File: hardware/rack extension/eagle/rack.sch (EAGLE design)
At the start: 48 parts, among them IC1 74ACT139N, IC2 74AC574N, IC3 74AC32N, IC4 74AC86N, IC5 74AC04N, IC6 74AC14N, IC7 74AC541N, K1 APF30212C, K2 APF30212C, Q1 BC547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

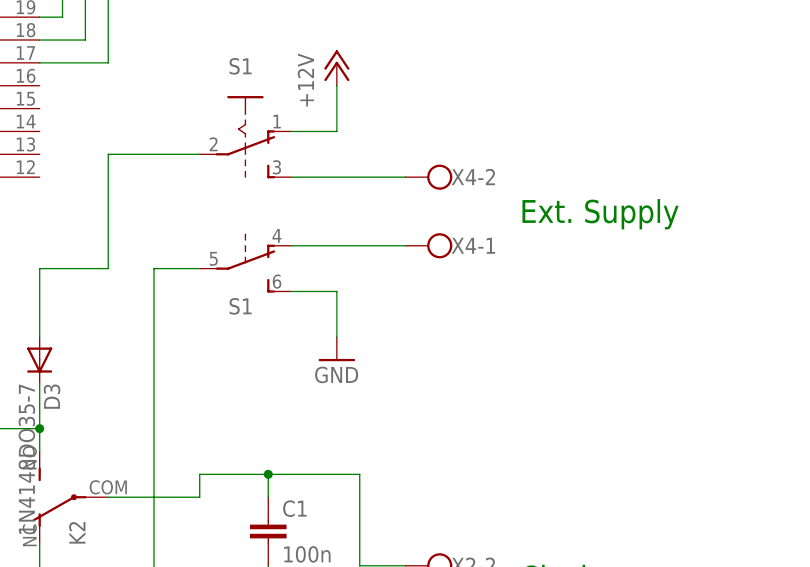
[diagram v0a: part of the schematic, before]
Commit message: Bad fail in rack hardware
The switch S1 was connected wrong so the change from internal to
external supply didnt work.
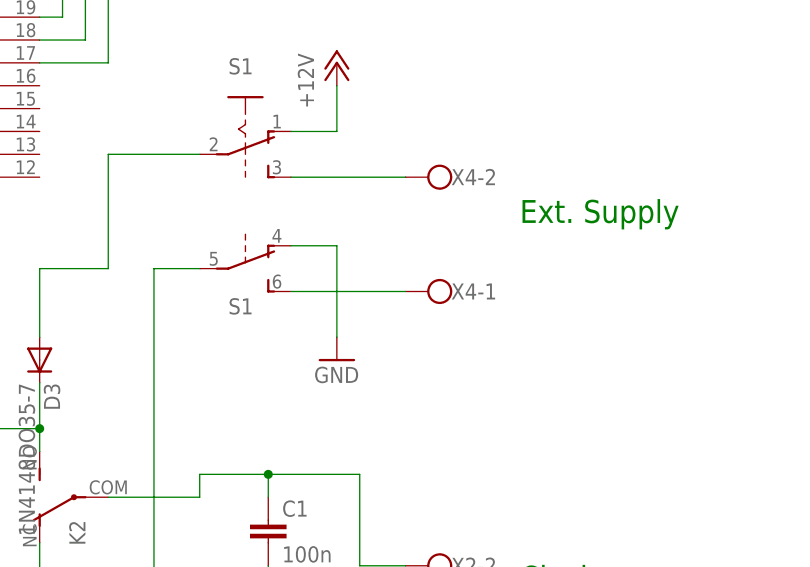
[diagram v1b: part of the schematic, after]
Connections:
- net GND: now also S1B.O; no longer S1B.S
- net N$33: now also S1B.S; no longer S1B.O
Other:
- moved on the sheet: X4-1
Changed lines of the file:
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@@
 <instance part="S1" gate="B" x="195.58" y="53.34" rot="R270"/>
 <instance part="S1" gate="A" x="195.58" y="68.58" rot="R270"/>
-<instance part="X4" gate="-1" x="218.44" y="55.88" rot="R180"/>
+<instance part="X4" gate="-1" x="218.44" y="50.8" rot="R180"/>
 <instance part="X4" gate="-2" x="218.44" y="63.5" rot="R180"/>
 <instance part="P+9" gate="1" x="152.4" y="27.94"/>
@@
 </segment>
 <segment>
-<pinref part="S1" gate="B" pin="S"/>
 <pinref part="GND9" gate="1" pin="GND"/>
-<wire x1="200.66" y1="50.8" x2="205.74" y2="50.8" width="0.1524" layer="91"/>
-<wire x1="205.74" y1="50.8" x2="205.74" y2="45.72" width="0.1524" layer="91"/>
+<wire x1="205.74" y1="45.72" x2="205.74" y2="55.88" width="0.1524" layer="91"/>
+<pinref part="S1" gate="B" pin="O"/>
+<wire x1="205.74" y1="55.88" x2="200.66" y2="55.88" width="0.1524" layer="91"/>
 </segment>
 <segment>
@@
 </segment>
 </net>
-<net name="N$33" class="0">
-<segment>
-<pinref part="S1" gate="B" pin="O"/>
-<pinref part="X4" gate="-1" pin="KL"/>
-<wire x1="200.66" y1="55.88" x2="213.36" y2="55.88" width="0.1524" layer="91"/>
-</segment>
-</net>
 <net name="N$34" class="0">
 <segment>
@@
 </segment>
 </net>
+<net name="N$33" class="0">
+<segment>
+<pinref part="S1" gate="B" pin="S"/>
+<pinref part="X4" gate="-1" pin="KL"/>
+<wire x1="200.66" y1="50.8" x2="213.36" y2="50.8" width="0.1524" layer="91"/>
+</segment>
+</net>

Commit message: Layout updated
Updated layout from rack extension
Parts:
- removed SV2: (no value), con-lstb:MA03-2
- added SV5: (no value), con-lstb:MA03-1
- C8: value (none) -> 2µ2
- IC1: value 74ACT139N -> 74HC139N; device 74xx-eu:74ACT139N -> 74xx-eu:74HC139N
- IC2: value 74AC574N -> 74HC574N; device 74xx-eu:74AC574N -> 74xx-eu:74HC574N
- IC3: value 74AC32N -> 74HC32N; device 74xx-eu:74AC32N -> 74xx-eu:74HC32N
- IC4: value 74AC86N -> 74HC86N; device 74xx-eu:74AC86N -> 74xx-eu:74HC86N
- IC5: value 74AC04N -> 74HC04N; device 74xx-eu:74AC04N -> 74xx-eu:74HC04N
- IC6: value 74AC14N -> 74HC14N; device 74xx-eu:74AC14N -> 74xx-eu:74HC14N
- IC7: value 74AC541N -> 74HC541N; device 74xx-eu:74AC541N -> 74xx-eu:74HC541N
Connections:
- net N$36: now also SV5.2; no longer SV2.3, SV2.5
- net N$6: now also SV5.3; no longer SV2.4
- net N$7: now also SV5.1; no longer SV2.6
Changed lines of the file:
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@@
 <part name="K1" library="relay" deviceset="APF30212C" device=""/>
 <part name="K2" library="relay" deviceset="APF30212C" device=""/>
-<part name="IC1" library="74xx-eu" deviceset="74*139" device="N" technology="ACT"/>
+<part name="IC1" library="74xx-eu" deviceset="74*139" device="N" technology="HC" value="74HC139N"/>
 <part name="P+1" library="supply1" deviceset="VCC" device=""/>
 <part name="P+2" library="supply1" deviceset="VCC" device=""/>
@@
 <part name="GND1" library="supply1" deviceset="GND" device=""/>
 <part name="GND2" library="supply1" deviceset="GND" device=""/>
-<part name="IC2" library="74xx-eu" deviceset="74*574" device="N" technology="AC"/>
+<part name="IC2" library="74xx-eu" deviceset="74*574" device="N" technology="HC" value="74HC574N"/>
 <part name="GND3" library="supply1" deviceset="GND" device=""/>
-<part name="IC3" library="74xx-eu" deviceset="74*32" device="N" technology="AC"/>
+<part name="IC3" library="74xx-eu" deviceset="74*32" device="N" technology="HC" value="74HC32N"/>
 <part name="GND4" library="supply1" deviceset="GND" device=""/>
 <part name="GND5" library="supply1" deviceset="GND" device=""/>
@@
 <part name="Q2" library="transistor-npn" deviceset="BC547*" device=""/>
 <part name="SV1" library="con-lstb" deviceset="MA04-2" device=""/>
-<part name="SV2" library="con-lstb" deviceset="MA03-2" device=""/>
 <part name="GND7" library="supply1" deviceset="GND" device=""/>
 <part name="P+5" library="supply1" deviceset="VCC" device=""/>
@@
 <part name="C7" library="rcl" deviceset="CPOL-EU" device="TT2D5" value="10uF/16V"/>
 <part name="D3" library="diode" deviceset="1N4148" device="DO35-7"/>
-<part name="IC4" library="74xx-eu" deviceset="74*86" device="N" technology="AC"/>
-<part name="IC5" library="74xx-eu" deviceset="74*04" device="N" technology="AC"/>
-<part name="IC6" library="74xx-eu" deviceset="74*14" device="N" technology="AC"/>
-<part name="C8" library="rcl" deviceset="CPOL-EU" device="E2,5-6E"/>
+<part name="IC4" library="74xx-eu" deviceset="74*86" device="N" technology="HC" value="74HC86N"/>
+<part name="IC5" library="74xx-eu" deviceset="74*04" device="N" technology="HC" value="74HC04N"/>
+<part name="IC6" library="74xx-eu" deviceset="74*14" device="N" technology="HC" value="74HC14N"/>
+<part name="C8" library="rcl" deviceset="CPOL-EU" device="E2,5-6E" value="2µ2"/>
 <part name="R6" library="rcl" deviceset="R-EU_" device="0204/7" value="270"/>
 <part name="SV3" library="con-lstb" deviceset="MA03-1" device=""/>
@@
 <part name="P+9" library="supply1" deviceset="+12V" device=""/>
 <part name="SV4" library="con-lstb" deviceset="MA03-1" device=""/>
-<part name="IC7" library="74xx-eu" deviceset="74*541" device="N" technology="AC"/>
+<part name="IC7" library="74xx-eu" deviceset="74*541" device="N" technology="HC" value="74HC541N"/>
 <part name="C12" library="rcl" deviceset="C-EU" device="050-024X044" value="100n"/>
 <part name="R9" library="rcl" deviceset="R-EU_" device="0204/7" value="390"/>
 <part name="LED4" library="led" deviceset="LED" device="B155"/>
 <part name="GND13" library="supply1" deviceset="GND" device=""/>
+<part name="SV5" library="con-lstb" deviceset="MA03-1" device=""/>
 </parts>
 <sheets>
@@
 <instance part="Q2" gate="G$1" x="167.64" y="109.22" rot="MR180"/>
 <instance part="SV1" gate="G$1" x="104.14" y="68.58"/>
-<instance part="SV2" gate="1" x="104.14" y="45.72"/>
 <instance part="GND7" gate="1" x="160.02" y="121.92" rot="R270"/>
 <instance part="P+5" gate="VCC" x="22.86" y="220.98"/>
@@
 <instance part="LED4" gate="G$1" x="208.28" y="175.26" rot="R90"/>
 <instance part="GND13" gate="1" x="116.84" y="111.76"/>
+<instance part="SV5" gate="G$1" x="104.14" y="35.56" rot="R90"/>
 </instances>
 <busses>
@@
 <segment>
 <pinref part="IC1" gate="B" pin="Y1"/>
-<wire x1="96.52" y1="45.72" x2="93.98" y2="45.72" width="0.1524" layer="91"/>
-<pinref part="SV2" gate="1" pin="4"/>
+<pinref part="SV5" gate="G$1" pin="3"/>
+<wire x1="93.98" y1="45.72" x2="101.6" y2="45.72" width="0.1524" layer="91"/>
+<wire x1="101.6" y1="45.72" x2="101.6" y2="43.18" width="0.1524" layer="91"/>
 </segment>
 </net>
@@
 <segment>
 <pinref part="IC1" gate="B" pin="Y0"/>
-<pinref part="SV2" gate="1" pin="6"/>
-<wire x1="93.98" y1="48.26" x2="96.52" y2="48.26" width="0.1524" layer="91"/>
+<pinref part="SV5" gate="G$1" pin="1"/>
+<wire x1="93.98" y1="48.26" x2="106.68" y2="48.26" width="0.1524" layer="91"/>
+<wire x1="106.68" y1="48.26" x2="106.68" y2="43.18" width="0.1524" layer="91"/>
 </segment>
 </net>
@@
 <net name="N$36" class="0">
 <segment>
-<pinref part="SV2" gate="1" pin="3"/>
-<pinref part="SV2" gate="1" pin="5"/>
-<wire x1="116.84" y1="48.26" x2="111.76" y2="48.26" width="0.1524" layer="91"/>
-<wire x1="116.84" y1="48.26" x2="116.84" y2="55.88" width="0.1524" layer="91"/>
+<wire x1="116.84" y1="45.72" x2="116.84" y2="55.88" width="0.1524" layer="91"/>
 <pinref part="IC3" gate="A" pin="I1"/>
 <wire x1="116.84" y1="55.88" x2="121.92" y2="55.88" width="0.1524" layer="91"/>
-<wire x1="111.76" y1="45.72" x2="116.84" y2="45.72" width="0.1524" layer="91"/>
-<wire x1="116.84" y1="45.72" x2="116.84" y2="48.26" width="0.1524" layer="91"/>
-<junction x="116.84" y="48.26"/>
 <wire x1="116.84" y1="55.88" x2="116.84" y2="81.28" width="0.1524" layer="91"/>
 <wire x1="116.84" y1="81.28" x2="114.3" y2="81.28" width="0.1524" layer="91"/>
@@
 <wire x1="114.3" y1="81.28" x2="114.3" y2="83.82" width="0.1524" layer="91"/>
 <junction x="116.84" y="55.88"/>
-</segment>
-</net>
+<pinref part="SV5" gate="G$1" pin="2"/>
+<wire x1="116.84" y1="45.72" x2="104.14" y2="45.72" width="0.1524" layer="91"/>
+<wire x1="104.14" y1="45.72" x2="104.14" y2="43.18" width="0.1524" layer="91"/>
+</segment>
+</net>

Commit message: Litte changes in schematic and layout
Added further description and fixed an naming issue in schmematic
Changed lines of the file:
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@@
 <text x="0" y="205.74" size="2.54" layer="91">DCF77</text>
 <text x="-2.54" y="200.66" size="1.778" layer="91">+5V</text>
-<text x="-2.54" y="195.58" size="1.778" layer="91">GND</text>
-<text x="-2.54" y="190.5" size="1.778" layer="91">Signal</text>
+<text x="-2.54" y="189.484" size="1.778" layer="91">GND</text>
+<text x="-2.794" y="195.072" size="1.778" layer="91">Signal</text>
 <text x="226.06" y="17.78" size="2.54" layer="91">Clock</text>
 <text x="50.8" y="210.82" size="1.778" layer="91">Pull-Up</text>
@@
 <pinref part="X3" gate="-3" pin="KL"/>
 <wire x1="33.02" y1="195.58" x2="17.78" y2="195.58" width="0.1524" layer="91"/>
-</segment>
-</net>
+<junction x="33.02" y="195.58"/>
+</segment>
+</net>

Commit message: Value of PullUp from1k to 15k
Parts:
- R7: value 1k -> 15k
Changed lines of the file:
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@@
 <part name="R6" library="rcl" deviceset="R-EU_" device="0204/7" value="270"/>
 <part name="SV3" library="con-lstb" deviceset="MA03-1" device=""/>
-<part name="R7" library="rcl" deviceset="R-EU_" device="0204/7" value="1k"/>
+<part name="R7" library="rcl" deviceset="R-EU_" device="0204/7" value="15k"/>
 <part name="GND11" library="supply1" deviceset="GND" device=""/>
 <part name="C9" library="rcl" deviceset="C-EU" device="050-024X044" value="100n"/>
@@
 <wire x1="215.9" y1="175.26" x2="215.9" y2="167.64" width="0.1524" layer="91"/>
 <wire x1="213.36" y1="175.26" x2="215.9" y2="175.26" width="0.1524" layer="91"/>
+<junction x="215.9" y="175.26"/>
 </segment>
 <segment>
@@
 <wire x1="88.9" y1="172.72" x2="99.06" y2="172.72" width="0.1524" layer="91"/>
 <wire x1="88.9" y1="170.18" x2="88.9" y2="172.72" width="0.1524" layer="91"/>
-</segment>
-</net>
+<junction x="88.9" y="172.72"/>
+</segment>
+</net>
